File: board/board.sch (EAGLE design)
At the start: 59 parts, among them Q2 ULN2003AD

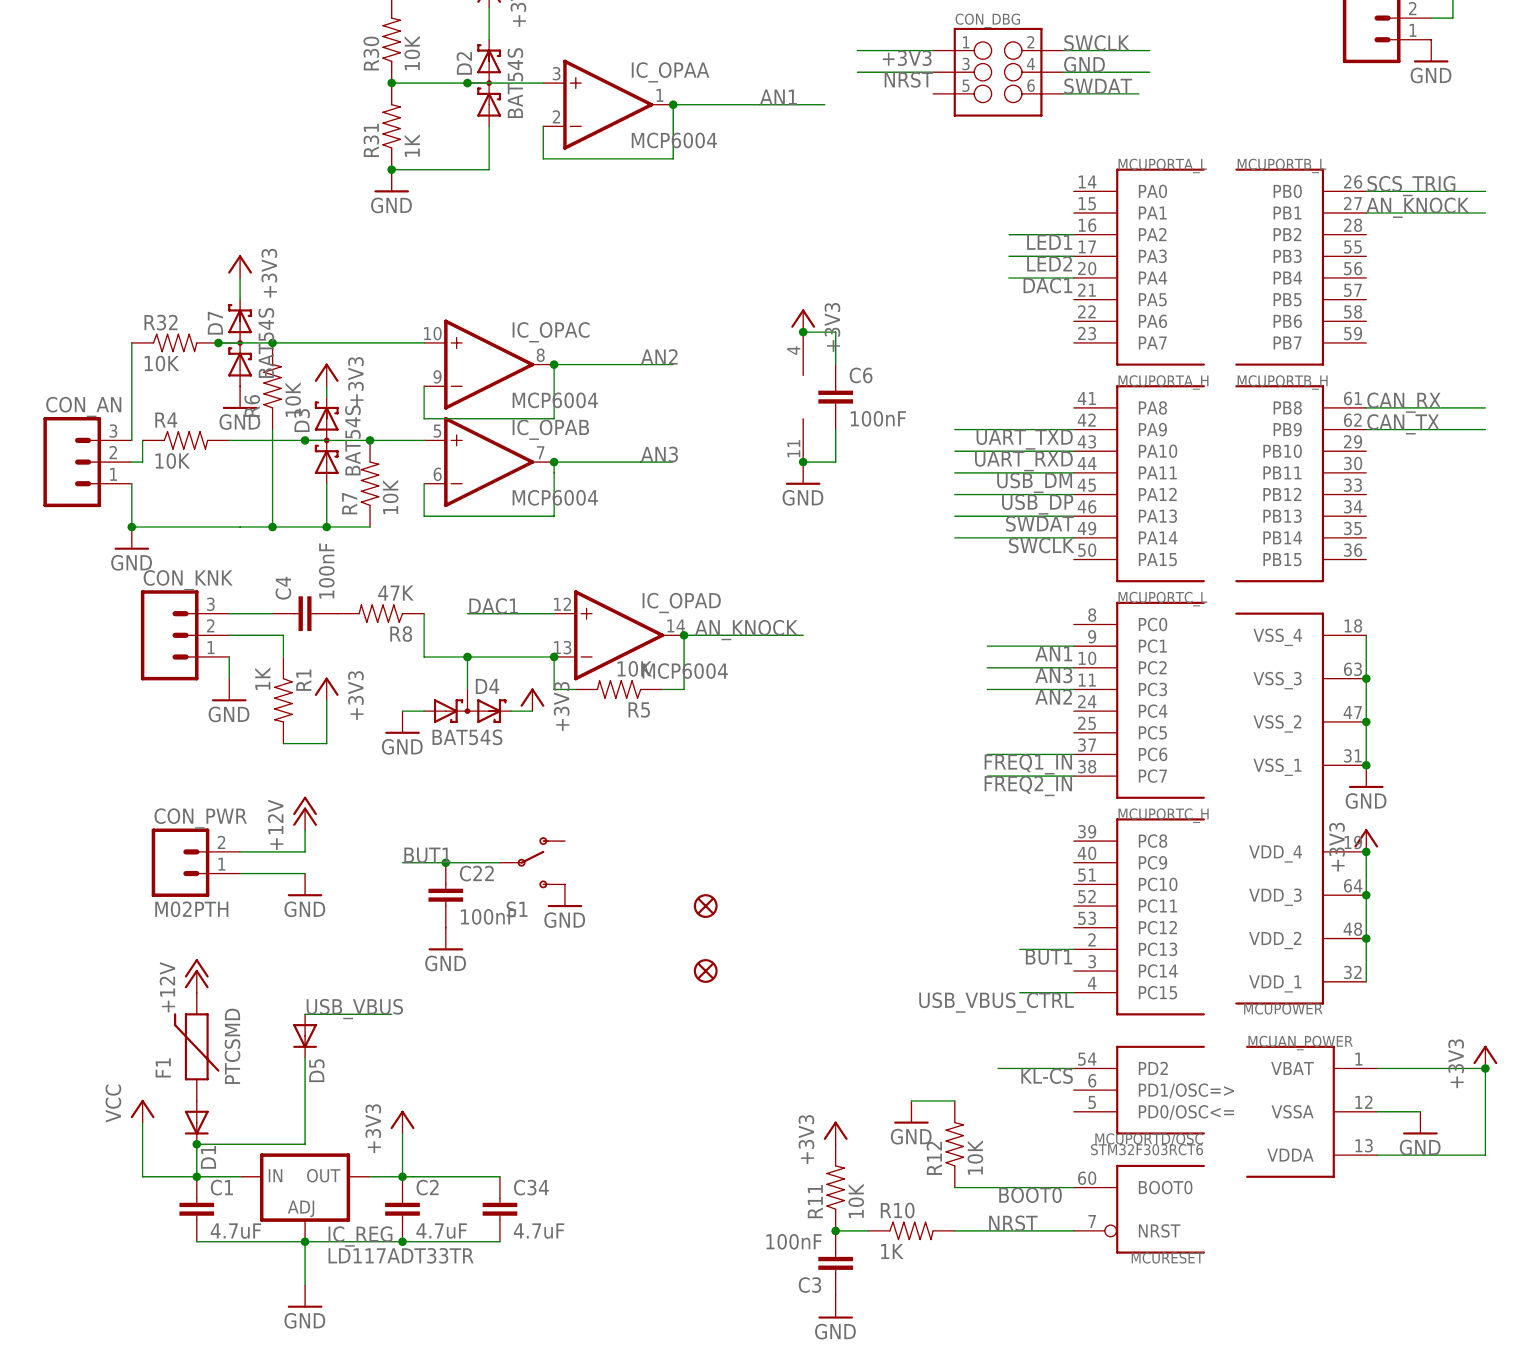
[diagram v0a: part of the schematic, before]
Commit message: Adding TVS Diode
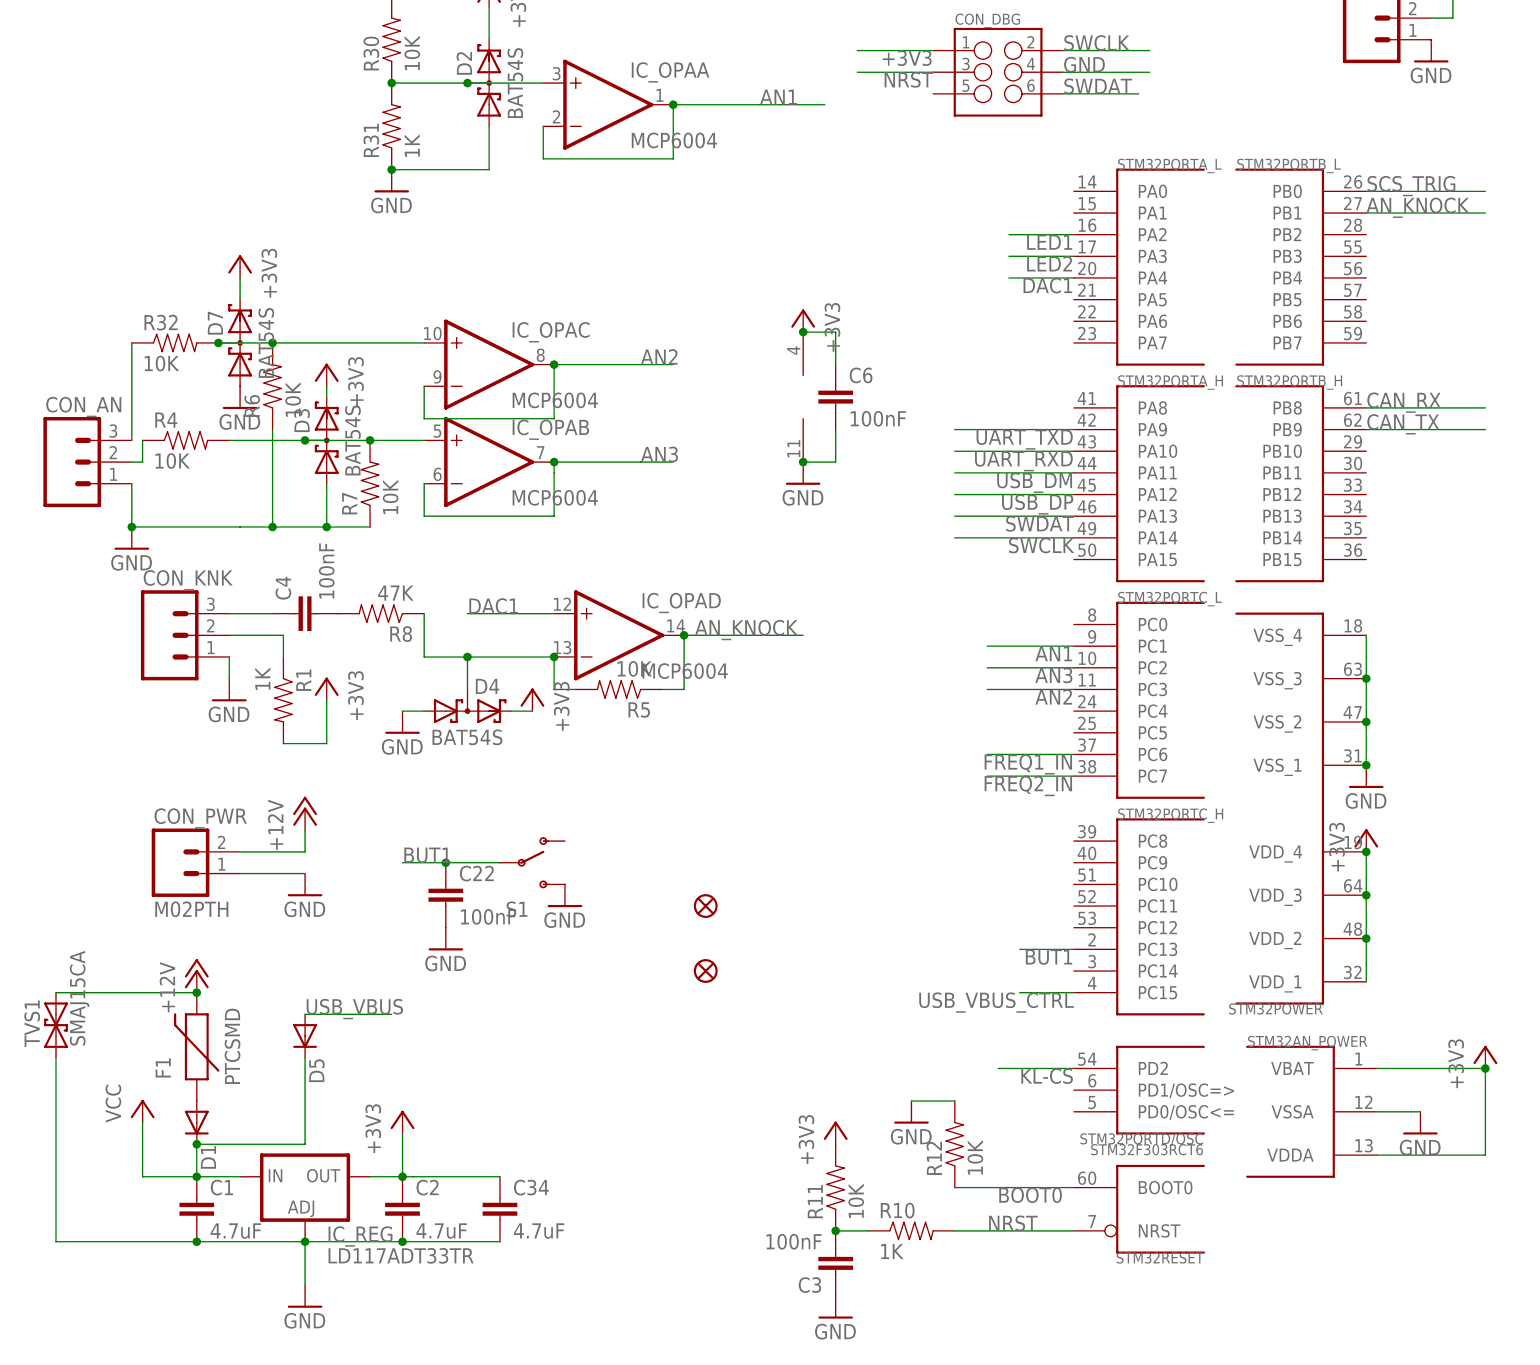
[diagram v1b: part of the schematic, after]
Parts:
- added TVS1: SMAJ15CA, SparkFun-DiscreteSemi:TVS
- renumbered MCU to STM32
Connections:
- net +12V: now also TVS1.2
- net GND: now also TVS1.1

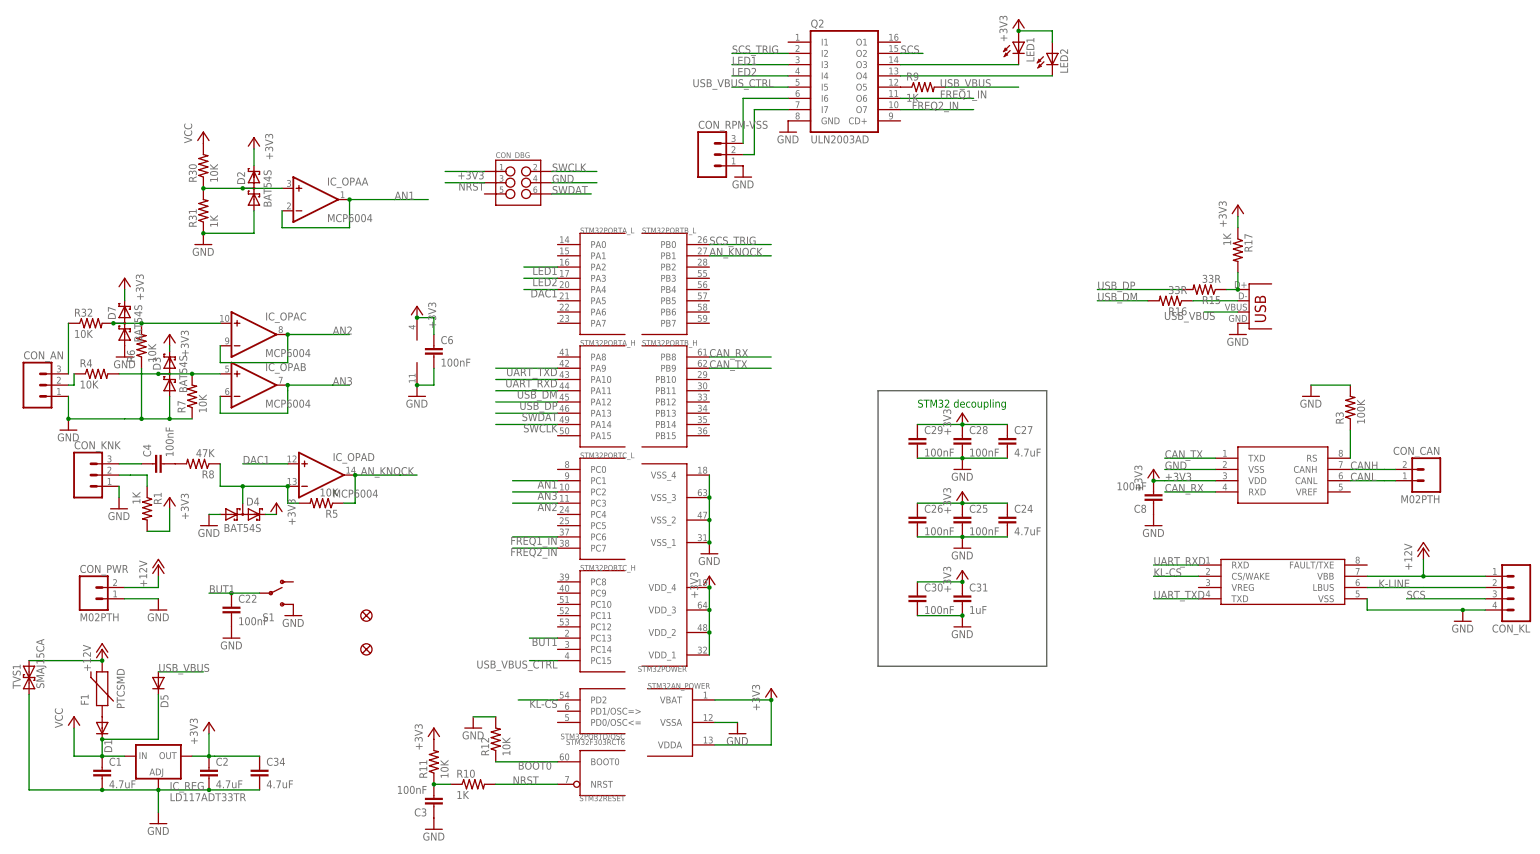
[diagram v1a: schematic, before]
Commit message: TVS Diode changes, Adding pull-ups to K-line, updated K-line IC
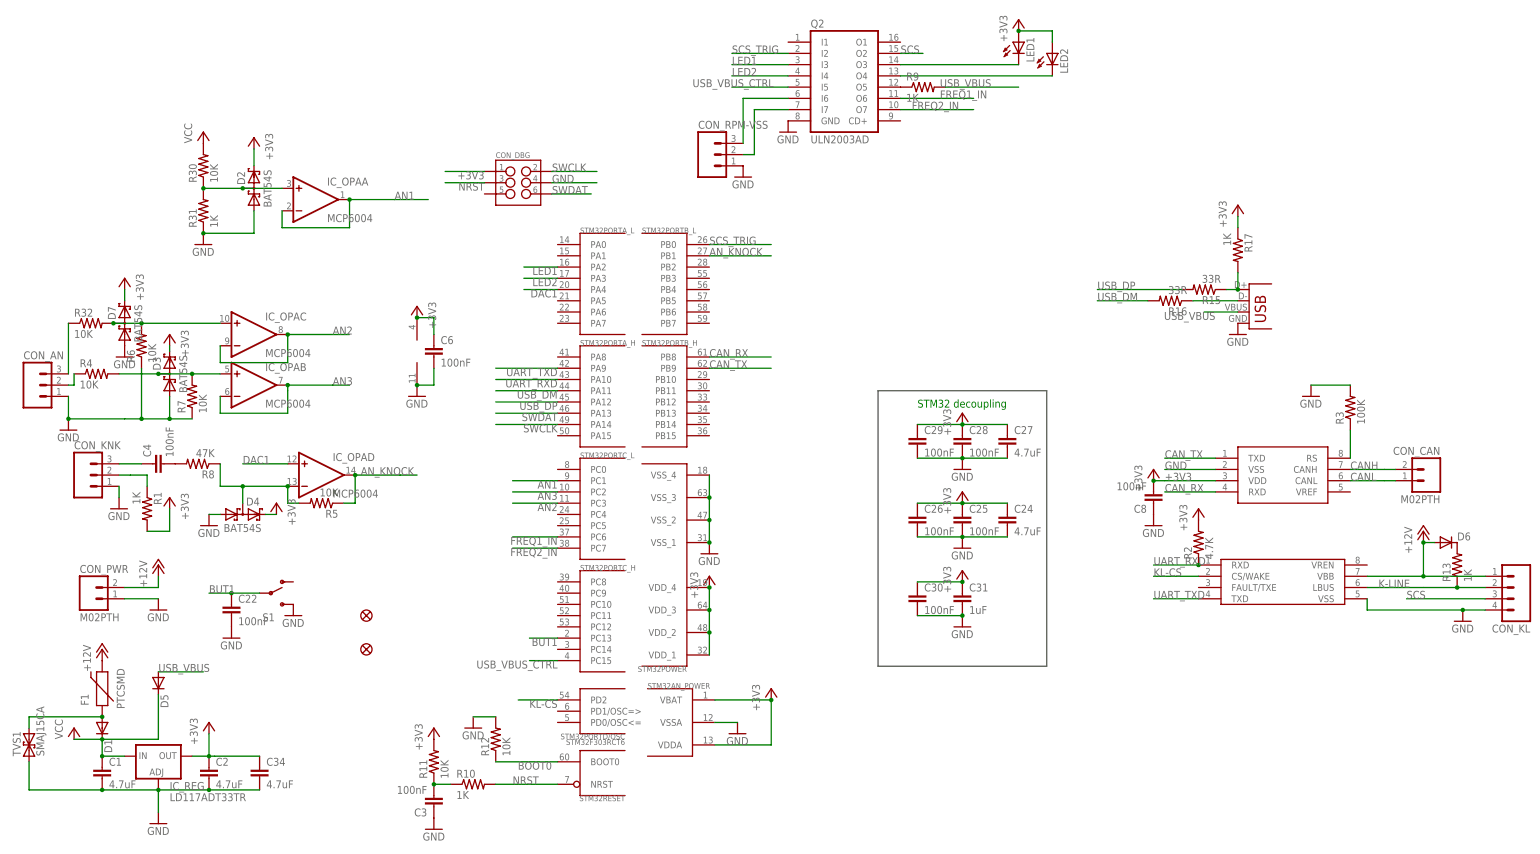
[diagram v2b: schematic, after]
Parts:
- removed IC_KL: MCP2004, misc:MCP2021
- added D6: (no value), SparkFun-DiscreteSemi:DIODESMA
- added IC_KLINE: MCP2004, misc:MCP2004
- added R13: 1K, SparkFun-Resistors:RESISTOR0603-RES
- added R2: 4.7K, SparkFun-Resistors:RESISTOR0603-RES
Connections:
- new net N$13: D6.C, R13.2
- net +12V: now also D6.A, IC_KLINE.VBB@7; no longer IC_KL.VBB@7, TVS1.2
- net +3V3: now also R2.2
- net GND: now also IC_KLINE.VSS@5; no longer IC_KL.VSS@5
- net K-LINE: now also IC_KLINE.LBUS@6, R13.1; no longer IC_KL.LBUS@6
- net KL-CS: now also IC_KLINE.CS/WAKE@2; no longer IC_KL.CS/WAKE@2
- net N$9: now also TVS1.2
- net UART_RXD: now also IC_KLINE.RXD@1, R2.1; no longer IC_KL.RXD@1
- net UART_TXD: now also IC_KLINE.TXD@4; no longer IC_KL.TXD@4
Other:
- moved on the sheet: TVS1

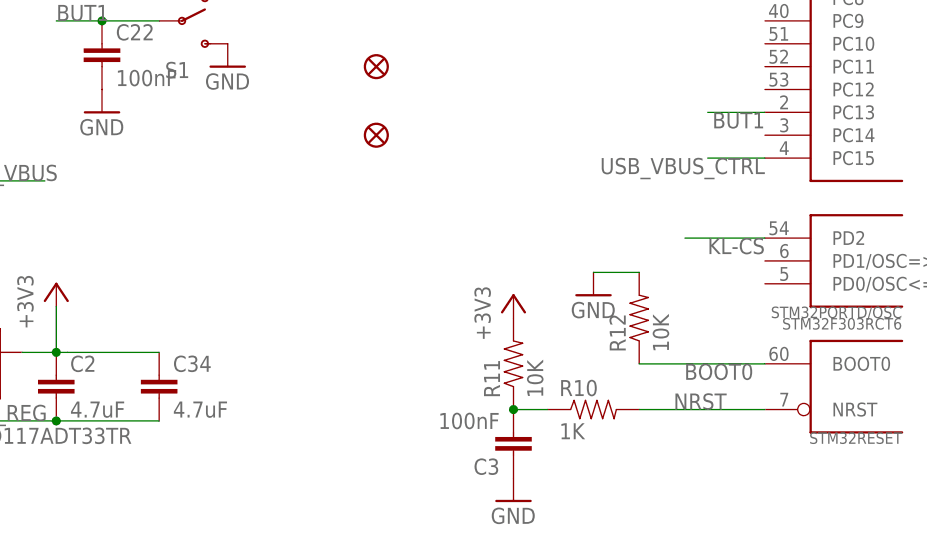
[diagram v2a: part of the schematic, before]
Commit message: Adding HSE Crystal, needed for USB.
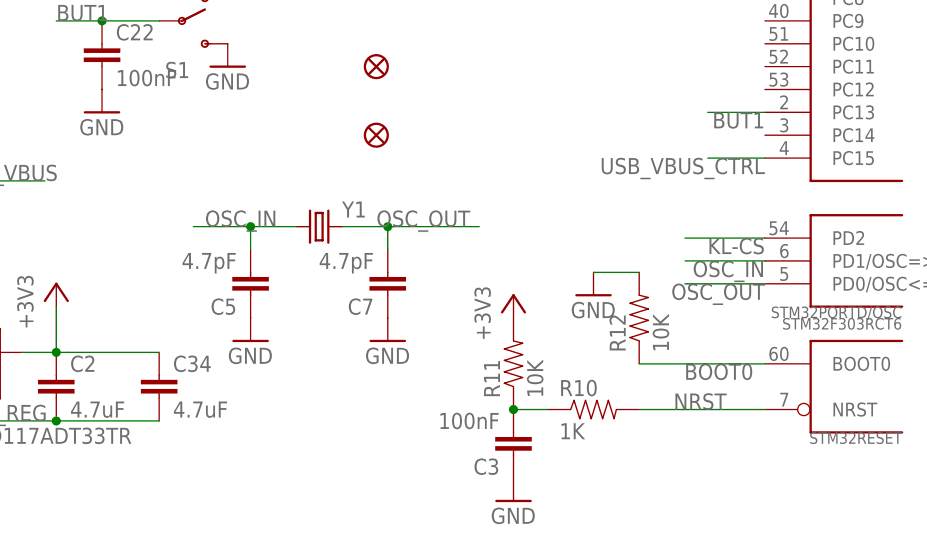
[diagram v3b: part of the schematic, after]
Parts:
- added C5, C7: 4.7pF, SparkFun-Capacitors:CAP0603-CAP
- added Y1: (no value), SparkFun-FreqCtrl:CRYSTALHC49US
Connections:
- new net OSC_IN: C5.2, STM32PORTD/OSC.PD1/OSC=>, Y1.1
- new net OSC_OUT: C7.2, STM32PORTD/OSC.PD0/OSC<=, Y1.2
- net GND: now also C5.1, C7.1
